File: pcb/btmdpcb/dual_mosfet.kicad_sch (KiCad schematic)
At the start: 4 parts, among them Q3 BSD235C

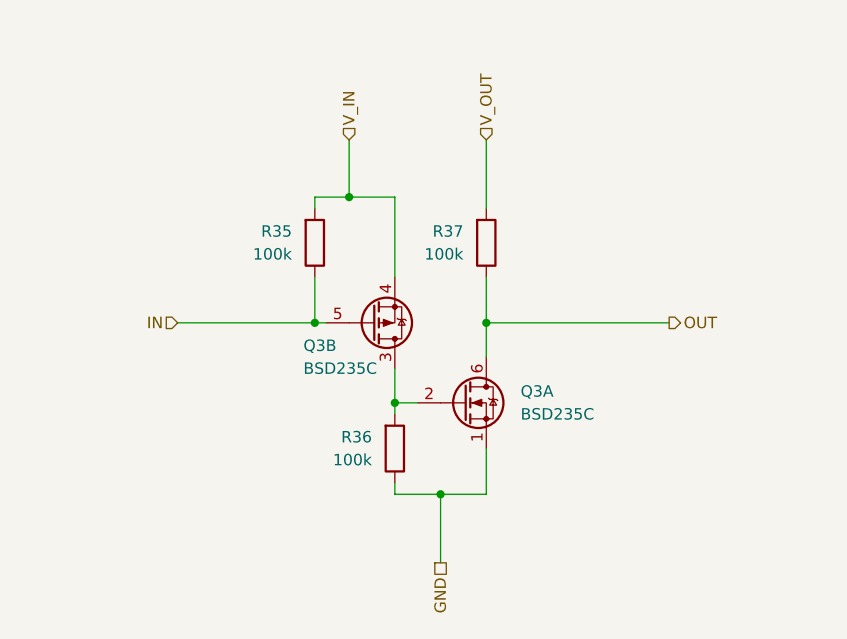
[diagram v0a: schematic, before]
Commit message: Clean up schematic, implement all logic functionality
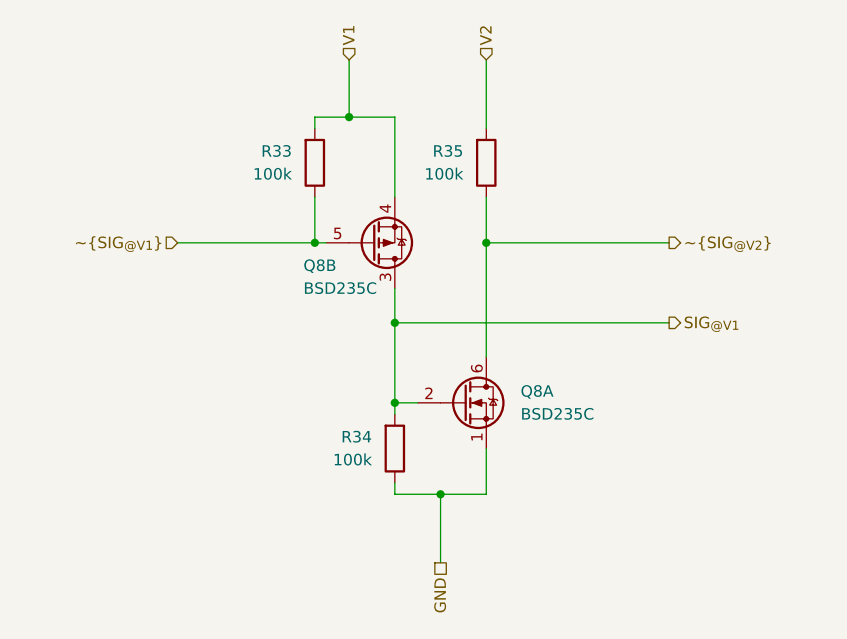
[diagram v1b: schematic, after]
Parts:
- renumbered Q3 to Q8, R35 to R33, R36 to R34, R37 to R35
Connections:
- net SIG_{@V1}: now reaches Q8.2 (GN), Q8.3 (DP), R34.2
- net IN renamed ~{SIG_{@V1}}
- net OUT renamed ~{SIG_{@V2}}
- net V_IN renamed V1
- net V_OUT renamed V2
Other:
- moved on the sheet: Q8B, R33, R35

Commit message: Remove redundant regulators, simplify schematic
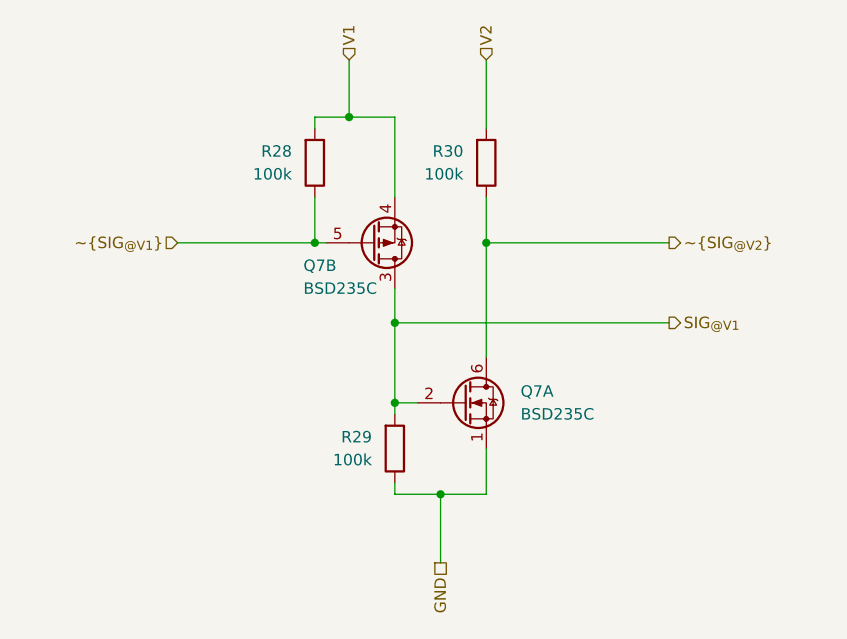
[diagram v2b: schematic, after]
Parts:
- renumbered Q8 to Q7, R33 to R28, R34 to R29, R35 to R30
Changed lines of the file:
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@@
 		(on_board yes)
 		(dnp no)
-		(property "Reference" "Q8"
+		(property "Reference" "Q7"
 			(at 104.14 71.12 0)
 			(effects
@@
 			(project "btmdpcb"
 				(path "/6e43e92f-e106-411c-86ee-217d084aee5b/187a6431-8efb-40fb-b2e6-980e8d4e9b0d"
+					(reference "Q7")
+					(unit 2)
+				)
+				(path "/6e43e92f-e106-411c-86ee-217d084aee5b/6fd51821-950e-4740-b3dd-116f45e482c2"
 					(reference "Q8")
-					(unit 2)
-				)
-				(path "/6e43e92f-e106-411c-86ee-217d084aee5b/6fd51821-950e-4740-b3dd-116f45e482c2"
-					(reference "Q9")
 					(unit 2)
 				)
@@
 		(dnp no)
 		(fields_autoplaced yes)
-		(property "Reference" "R34"
+		(property "Reference" "R29"
 			(at 111.76 90.1699 0)
 			(effects
@@
 			(project "btmdpcb"
 				(path "/6e43e92f-e106-411c-86ee-217d084aee5b/187a6431-8efb-40fb-b2e6-980e8d4e9b0d"
-					(reference "R34")
-					(unit 1)
-				)
-				(path "/6e43e92f-e106-411c-86ee-217d084aee5b/6fd51821-950e-4740-b3dd-116f45e482c2"
-					(reference "R37")
+					(reference "R29")
+					(unit 1)
+				)
+				(path "/6e43e92f-e106-411c-86ee-217d084aee5b/6fd51821-950e-4740-b3dd-116f45e482c2"
+					(reference "R32")
 					(unit 1)
 				)
@@
 		(dnp no)
 		(fields_autoplaced yes)
-		(property "Reference" "Q8"
+		(property "Reference" "Q7"
 			(at 128.27 85.0899 0)
 			(effects
@@
 			(project "btmdpcb"
 				(path "/6e43e92f-e106-411c-86ee-217d084aee5b/187a6431-8efb-40fb-b2e6-980e8d4e9b0d"
+					(reference "Q7")
+					(unit 1)
+				)
+				(path "/6e43e92f-e106-411c-86ee-217d084aee5b/6fd51821-950e-4740-b3dd-116f45e482c2"
 					(reference "Q8")
-					(unit 1)
-				)
-				(path "/6e43e92f-e106-411c-86ee-217d084aee5b/6fd51821-950e-4740-b3dd-116f45e482c2"
-					(reference "Q9")
 					(unit 1)
 				)
@@
 		(dnp no)
 		(fields_autoplaced yes)
-		(property "Reference" "R33"
+		(property "Reference" "R28"
 			(at 102.87 58.4199 0)
 			(effects
@@
 			(project "btmdpcb"
 				(path "/6e43e92f-e106-411c-86ee-217d084aee5b/187a6431-8efb-40fb-b2e6-980e8d4e9b0d"
-					(reference "R33")
-					(unit 1)
-				)
-				(path "/6e43e92f-e106-411c-86ee-217d084aee5b/6fd51821-950e-4740-b3dd-116f45e482c2"
-					(reference "R36")
+					(reference "R28")
+					(unit 1)
+				)
+				(path "/6e43e92f-e106-411c-86ee-217d084aee5b/6fd51821-950e-4740-b3dd-116f45e482c2"
+					(reference "R31")
 					(unit 1)
 				)
@@
 		(dnp no)
 		(fields_autoplaced yes)
-		(property "Reference" "R35"
+		(property "Reference" "R30"
 			(at 121.92 58.4199 0)
 			(effects
@@
 			(project "btmdpcb"
 				(path "/6e43e92f-e106-411c-86ee-217d084aee5b/187a6431-8efb-40fb-b2e6-980e8d4e9b0d"
-					(reference "R35")
-					(unit 1)
-				)
-				(path "/6e43e92f-e106-411c-86ee-217d084aee5b/6fd51821-950e-4740-b3dd-116f45e482c2"
-					(reference "R38")
-					(unit 1)
-				)
+					(reference "R30")
+					(unit 1)
+				)
+				(path "/6e43e92f-e106-411c-86ee-217d084aee5b/6fd51821-950e-4740-b3dd-116f45e482c2"
+					(reference "R33")
+					(unit 1)
+				)

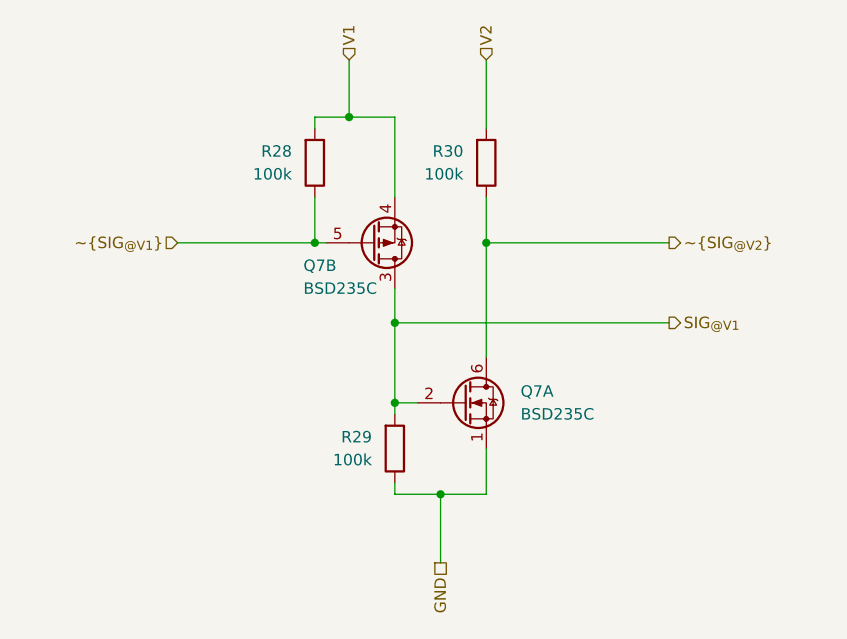
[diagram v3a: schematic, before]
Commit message: Add BT auto-powerup (RC circuit + comparator)
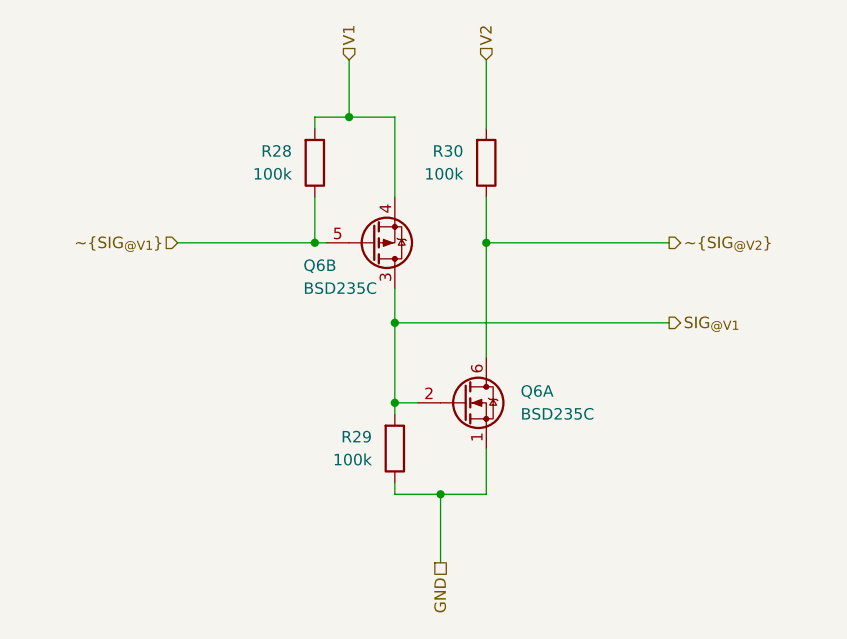
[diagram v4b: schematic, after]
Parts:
- renumbered Q7 to Q6
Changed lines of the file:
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@@
 		(on_board yes)
 		(dnp no)
-		(property "Reference" "Q7"
+		(property "Reference" "Q6"
 			(at 104.14 71.12 0)
 			(effects
@@
 			(project "btmdpcb"
 				(path "/6e43e92f-e106-411c-86ee-217d084aee5b/187a6431-8efb-40fb-b2e6-980e8d4e9b0d"
-					(reference "Q7")
+					(reference "Q6")
 					(unit 2)
 				)
@@
 		(dnp no)
 		(fields_autoplaced yes)
-		(property "Reference" "Q7"
+		(property "Reference" "Q6"
 			(at 128.27 85.0899 0)
 			(effects
@@
 			(project "btmdpcb"
 				(path "/6e43e92f-e106-411c-86ee-217d084aee5b/187a6431-8efb-40fb-b2e6-980e8d4e9b0d"
-					(reference "Q7")
+					(reference "Q6")
 					(unit 1)
 				)

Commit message: Add missing libraries, assign all footprints
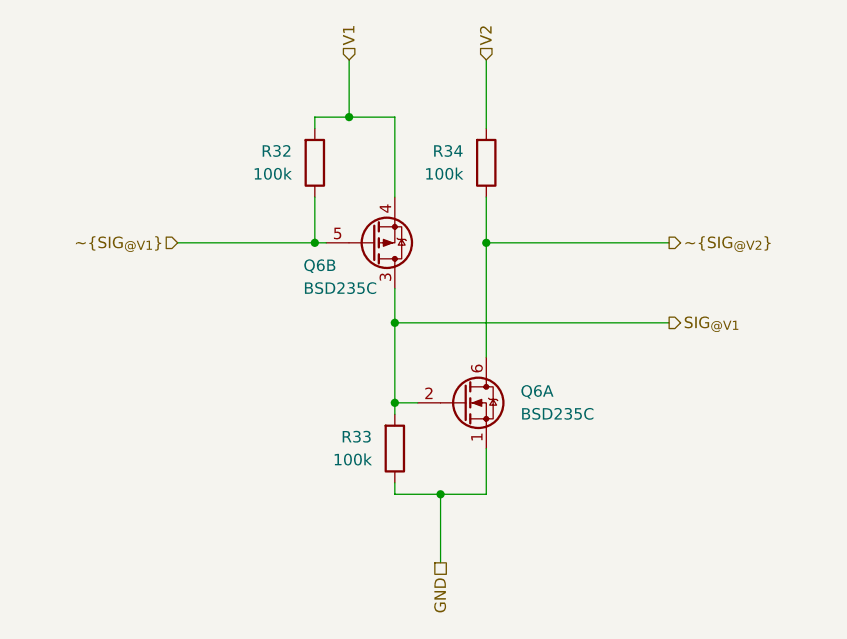
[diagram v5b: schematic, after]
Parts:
- R32: renamed from R28; footprint (none) -> Resistor_SMD:R_0805_2012Metric_Pad1.20x1.40mm_HandSolder
- R33: renamed from R29; footprint (none) -> Resistor_SMD:R_0805_2012Metric_Pad1.20x1.40mm_HandSolder
- R34: renamed from R30; footprint (none) -> Resistor_SMD:R_0805_2012Metric_Pad1.20x1.40mm_HandSolder
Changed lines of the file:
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@@
 		(dnp no)
 		(fields_autoplaced yes)
-		(property "Reference" "R29"
+		(property "Reference" "R33"
 			(at 111.76 90.1699 0)
 			(effects
@@
 			)
 		)
-		(property "Footprint" ""
+		(property "Footprint" "Resistor_SMD:R_0805_2012Metric_Pad1.20x1.40mm_HandSolder"
 			(at 112.522 91.44 90)
 			(effects
@@
 			(project "btmdpcb"
 				(path "/6e43e92f-e106-411c-86ee-217d084aee5b/187a6431-8efb-40fb-b2e6-980e8d4e9b0d"
-					(reference "R29")
+					(reference "R33")
 					(unit 1)
 				)
@@
 		(dnp no)
 		(fields_autoplaced yes)
-		(property "Reference" "R28"
+		(property "Reference" "R32"
 			(at 102.87 58.4199 0)
 			(effects
@@
 			)
 		)
-		(property "Footprint" ""
+		(property "Footprint" "Resistor_SMD:R_0805_2012Metric_Pad1.20x1.40mm_HandSolder"
 			(at 103.632 59.69 90)
 			(effects
@@
 			(project "btmdpcb"
 				(path "/6e43e92f-e106-411c-86ee-217d084aee5b/187a6431-8efb-40fb-b2e6-980e8d4e9b0d"
-					(reference "R28")
+					(reference "R32")
 					(unit 1)
 				)
@@
 		(dnp no)
 		(fields_autoplaced yes)
-		(property "Reference" "R30"
+		(property "Reference" "R34"
 			(at 121.92 58.4199 0)
 			(effects
@@
 			)
 		)
-		(property "Footprint" ""
+		(property "Footprint" "Resistor_SMD:R_0805_2012Metric_Pad1.20x1.40mm_HandSolder"
 			(at 122.682 59.69 90)
 			(effects
@@
 			(project "btmdpcb"
 				(path "/6e43e92f-e106-411c-86ee-217d084aee5b/187a6431-8efb-40fb-b2e6-980e8d4e9b0d"
-					(reference "R30")
-					(unit 1)
-				)
+					(reference "R34")
+					(unit 1)
+				)

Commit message: Correct footprints, fix issues on update PCB from schematic
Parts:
- Q6: footprint Package_TO_SOT_SMD:SOT-363_SC-70-6 -> Package_TO_SOT_SMD:SOT-363_SC-70-6_Handsoldering
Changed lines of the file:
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@@
 			)
 		)
-		(property "Footprint" "Package_TO_SOT_SMD:SOT-363_SC-70-6"
+		(property "Footprint" "Package_TO_SOT_SMD:SOT-363_SC-70-6_Handsoldering"
 			(at 116.84 70.485 0)
 			(effects
@@
 			)
 		)
-		(property "Footprint" "Package_TO_SOT_SMD:SOT-363_SC-70-6"
+		(property "Footprint" "Package_TO_SOT_SMD:SOT-363_SC-70-6_Handsoldering"
 			(at 127 88.265 0)
 			(effects

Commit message: Layout PCB
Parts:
- renumbered R32 to R31, R33 to R32, R34 to R33
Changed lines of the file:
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@@
 		(dnp no)
 		(fields_autoplaced yes)
-		(property "Reference" "R33"
+		(property "Reference" "R32"
 			(at 111.76 90.1699 0)
 			(effects
@@
 			(project "btmdpcb"
 				(path "/6e43e92f-e106-411c-86ee-217d084aee5b/187a6431-8efb-40fb-b2e6-980e8d4e9b0d"
-					(reference "R33")
+					(reference "R32")
 					(unit 1)
 				)
@@
 		(dnp no)
 		(fields_autoplaced yes)
-		(property "Reference" "R32"
+		(property "Reference" "R31"
 			(at 102.87 58.4199 0)
 			(effects
@@
 			(project "btmdpcb"
 				(path "/6e43e92f-e106-411c-86ee-217d084aee5b/187a6431-8efb-40fb-b2e6-980e8d4e9b0d"
-					(reference "R32")
+					(reference "R31")
 					(unit 1)
 				)
@@
 		(dnp no)
 		(fields_autoplaced yes)
-		(property "Reference" "R34"
+		(property "Reference" "R33"
 			(at 121.92 58.4199 0)
 			(effects
@@
 			(project "btmdpcb"
 				(path "/6e43e92f-e106-411c-86ee-217d084aee5b/187a6431-8efb-40fb-b2e6-980e8d4e9b0d"
-					(reference "R34")
-					(unit 1)
-				)
+					(reference "R33")
+					(unit 1)
+				)
